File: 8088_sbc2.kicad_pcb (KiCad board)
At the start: 2 copper layers, 200 x 100 mm, 65 parts, among them P1 CONN_02X10, P2 JMP_USB_PWR, P3 USB_B, Q1 IRLML6402, SW1 SW_PUSH, U1 P8088, U11 74HC573, U12 74HC573, U13 74HC573, U14 74HC573, U15 74HC138, U16 74HC138, U17 74HC14_OWN, U18 74HC08, U19 74HC32, U2 28C64, U20 10xLEDBAR, U3 AS6C4008, U4 TL770xA, U5 16C550, U6 FT232RL, U7 OSC_SMALL

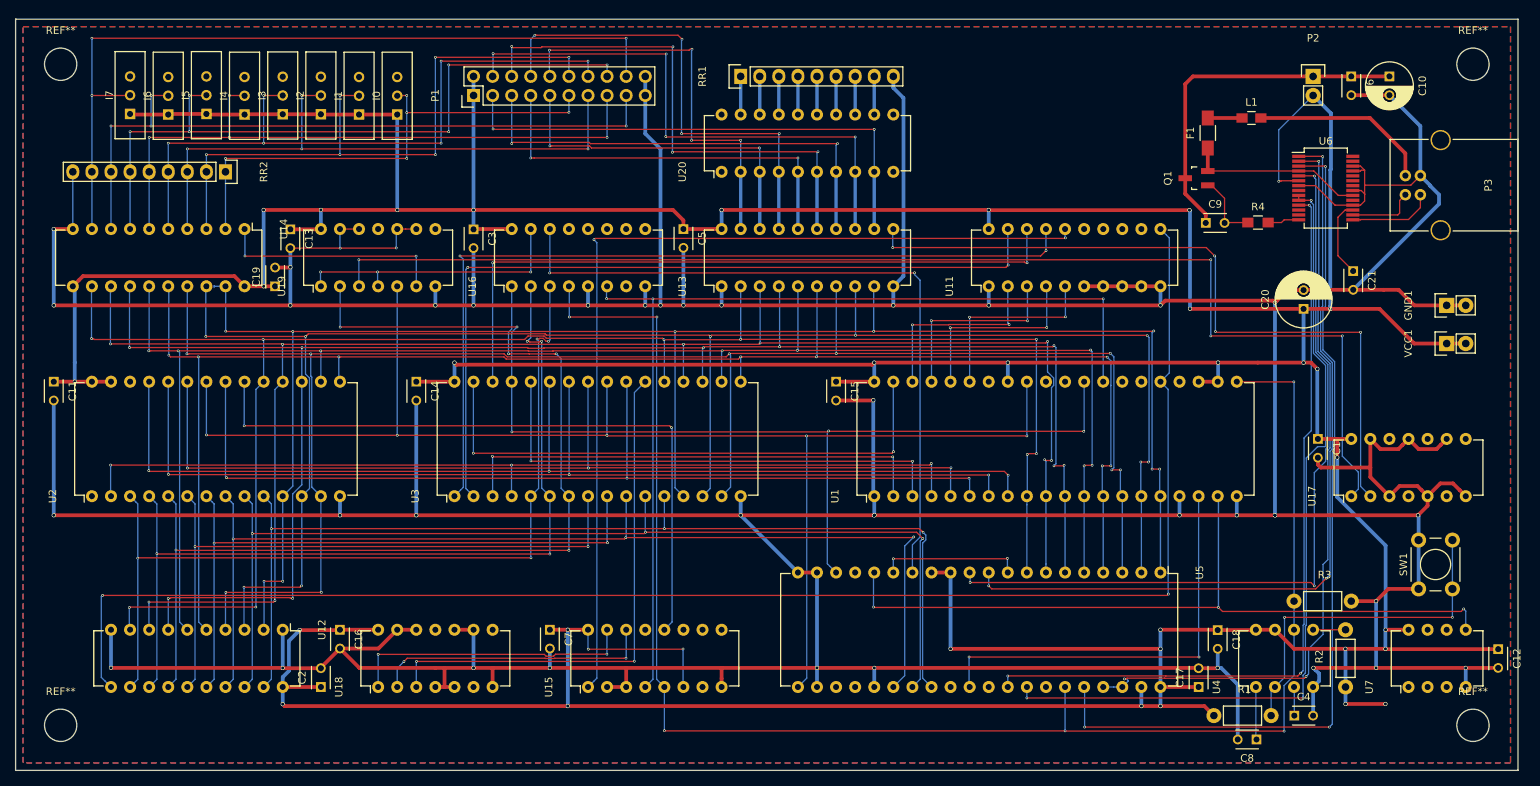
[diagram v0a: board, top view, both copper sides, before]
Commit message: version with new design rules
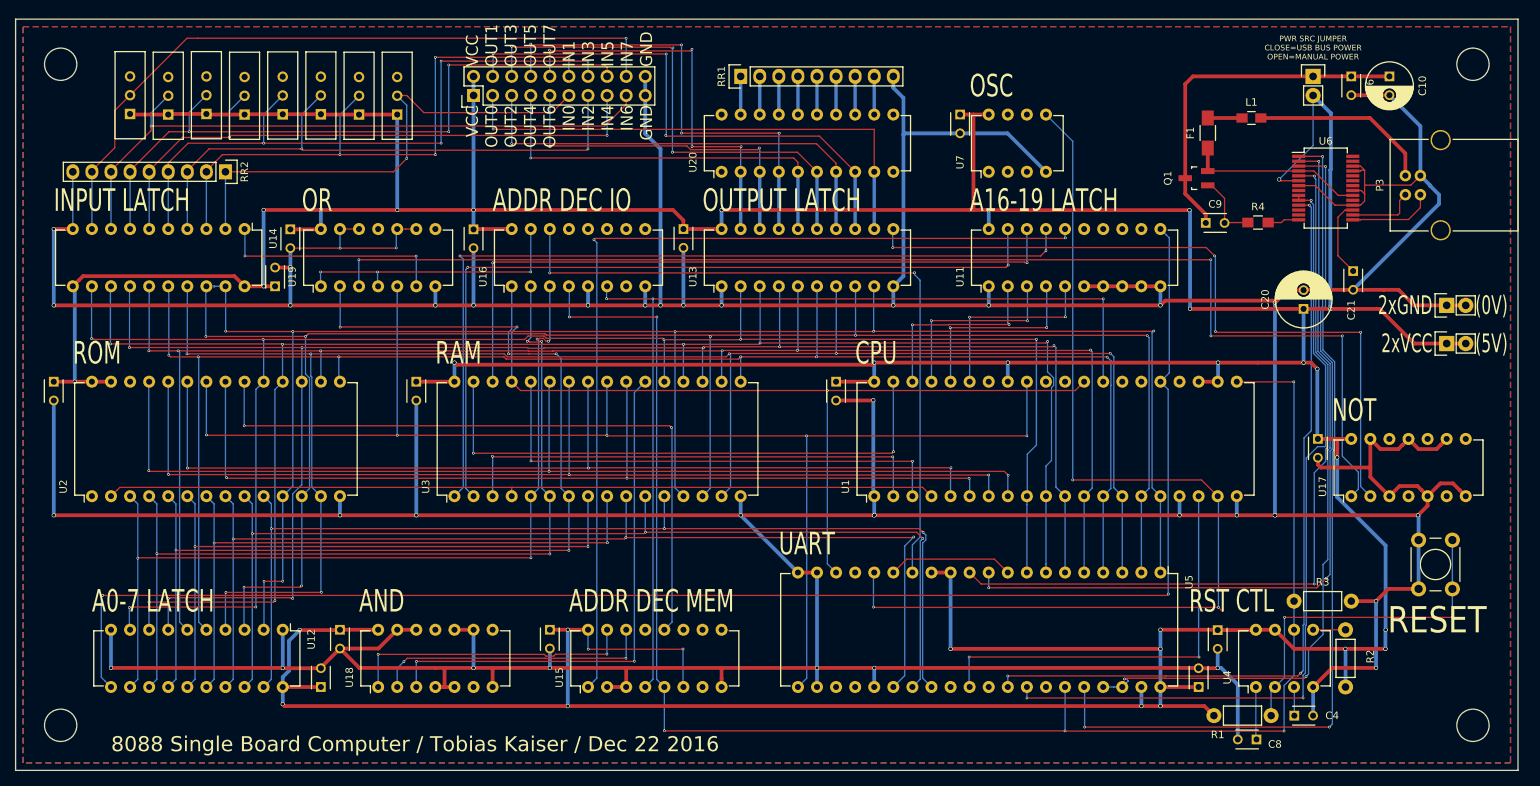
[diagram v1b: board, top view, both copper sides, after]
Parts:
- moved C12 101.0 mm to (175.7, 62.7)
- moved U7 88.5 mm to (179.5, 70.3)
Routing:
- net /CLK: track 101.3 -> 136.5 mm
- net /IN7: track 106.7 -> 94.2 mm, vias 3 -> 1
- net /A12: track 122.0 -> 111.5 mm, vias 3 -> 0
- net VCC: track 863.3 -> 853.9 mm, vias 35 -> 33
- net /nWR: track 145.5 -> 138.5 mm, vias 5 -> 3
- net /IN6: track 92.7 -> 86.6 mm, vias 4 -> 1
- net /IN5: track 94.0 -> 89.5 mm, vias 6 -> 3
- net /IN4: track 86.4 -> 82.4 mm, vias 4 -> 2
- net /IN2: track 80.8 -> 77.7 mm, vias 4 -> 2
- net /IN3: track 89.2 -> 86.1 mm, vias 6 -> 4
- net /OUT1: track 74.7 -> 71.9 mm, vias 4 -> 3
- net /IN1: track 84.1 -> 81.4 mm, vias 6 -> 4
- net Net-(U5-Pad15): track 18.9 -> 16.8 mm, vias 2 -> 0
- net /OUT2: track 61.4 -> 59.4 mm, vias 2 -> 1
- net /OUT3: track 69.4 -> 67.5 mm, vias 4 -> 3
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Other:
- net class Default: clearance 0.15 -> 0.16; trace_width 0.15 -> 0.16; via_dia 0.35 -> 0.45; via_drill 0.2 -> 0.3
- rule trace_clearance: 0.15 -> 0.16
- rule trace_min: 0.15 -> 0.16
- rule via_min_drill: 0.2 -> 0.3
- rule via_min_size: 0.35 -> 0.45
- board text added: "(0V)"
- board text added: "(5V)"
- board text added: "2xGND"
- board text added: "2xVCC"
- board text added: "8088 Single Board Computer / Tobias Kaiser / Dec 22 2016"
- board text added: "A0-7 LATCH"
- board text added: "A16-19 LATCH"
- board text added: "ADDR DEC IO"
- board text added: "ADDR DEC MEM"
- board text added: "AND"
- board text added: "CPU"
- board text added: "INPUT LATCH"
- board text added: "NOT"
- board text added: "OR"
- board text added: "OSC"
- board text added: "OUTPUT LATCH"
- board text added: "PWR SRC JUMPER CLOSE=USB BUS POWER OPEN=MANUAL POWER"
- board text added: "RAM"
- board text added: "RESET"
- board text added: "ROM"
- board text added: "RST CTL"
- board text added: "UART"
- board text added: "VCC OUT0 OUT2 OUT4 OUT6 IN0 IN2 IN4 IN6 GND"
- board text added: "VCC OUT1 OUT3 OUT5 OUT7 IN1 IN3 IN5 IN7 GND"

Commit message: test
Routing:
- net GND: track 1033.4 -> 0.00 mm, vias 38 -> 0
- net VCC: track 853.9 -> 0.00 mm, vias 33 -> 0
- net /D2: track 241.0 -> 0.00 mm, vias 7 -> 0
- net /D1: track 240.1 -> 0.00 mm, vias 7 -> 0
- net /D0: track 235.4 -> 0.00 mm, vias 7 -> 0
- net /D7: track 233.4 -> 0.00 mm, vias 7 -> 0
- net /D6: track 231.8 -> 0.00 mm, vias 7 -> 0
- net /D4: track 218.7 -> 0.00 mm, vias 6 -> 0
- net /D3: track 216.8 -> 0.00 mm, vias 6 -> 0
- net /RES: track 214.3 -> 0.00 mm, vias 6 -> 0
- net /ALE: track 204.8 -> 0.00 mm, vias 2 -> 0
- net /nRD: track 184.5 -> 0.00 mm, vias 5 -> 0
- net /nIODEV0_WREN: track 167.2 -> 0.00 mm, vias 4 -> 0
- net /A2: track 143.6 -> 0.00 mm, vias 3 -> 0
- net /A8: track 141.3 -> 0.00 mm, vias 3 -> 0
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- removed copper zone on B.Cu, net GND
- removed copper zone on F.Cu, net GND

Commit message: shitty kicad fucked it up while saving. fuck it.
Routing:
- net GND: track 0.00 -> 1033.4 mm, vias 0 -> 38
- net VCC: track 0.00 -> 853.9 mm, vias 0 -> 33
- net /D2: track 0.00 -> 241.0 mm, vias 0 -> 7
- net /D1: track 0.00 -> 240.1 mm, vias 0 -> 7
- net /D0: track 0.00 -> 235.4 mm, vias 0 -> 7
- net /D7: track 0.00 -> 233.4 mm, vias 0 -> 7
- net /D6: track 0.00 -> 231.8 mm, vias 0 -> 7
- net /D4: track 0.00 -> 218.7 mm, vias 0 -> 6
- net /D3: track 0.00 -> 216.8 mm, vias 0 -> 6
- net /RES: track 0.00 -> 214.3 mm, vias 0 -> 6
- net /ALE: track 0.00 -> 204.8 mm, vias 0 -> 2
- net /nRD: track 0.00 -> 184.5 mm, vias 0 -> 5
- net /nIODEV0_WREN: track 0.00 -> 167.2 mm, vias 0 -> 4
- net /A2: track 0.00 -> 143.6 mm, vias 0 -> 3
- net /A8: track 0.00 -> 141.3 mm, vias 0 -> 3
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- added copper zone on B.Cu, net GND
- added copper zone on F.Cu, net GND

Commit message: zwischenstand
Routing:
- net Net-(U5-Pad36): track 117.2 -> 38.5 mm, vias 3 -> 2
- net Net-(U5-Pad10): track 108.0 -> 51.5 mm
- net (no net): track 0.04 -> 5.97 mm
- net /A7: track 117.4 -> 115.9 mm, vias 4 -> 2
- net /A6: track 116.9 -> 116.2 mm
- net VCC: track 853.9 -> 854.5 mm, vias 33 -> 32
- net /A17: track 91.6 -> 92.1 mm
- removed copper zone on B.Cu, net GND
- removed copper zone on F.Cu, net GND

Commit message: zwischenstand2
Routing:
- net Net-(U5-Pad36): track 38.5 -> 115.8 mm, vias 2 -> 4
- net (no net): track 5.97 -> 0.04 mm
- net /ALE: track 204.8 -> 208.6 mm
- net Net-(U5-Pad37): track 102.1 -> 103.0 mm

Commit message: zwischenstand3
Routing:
- net VCC: track 854.5 -> 840.9 mm, vias 32 -> 26
- net GND: track 1033.6 -> 1027.5 mm, vias 38 -> 30
- net /OUT0: track 68.5 -> 64.6 mm
- net /A19: track 124.3 -> 122.3 mm, vias 2 -> 1
- net /D0: track 235.6 -> 233.8 mm
- net /nIODEV0_RDEN: track 30.4 -> 28.7 mm
- net /A12: track 111.5 -> 112.8 mm
- net /OUT7: track 53.1 -> 51.8 mm, vias 4 -> 2
- net /nIODEV0_EN: track 37.7 -> 36.7 mm, vias 3 -> 1
- net /OUT6: track 45.9 -> 44.9 mm, vias 2 -> 1
- net /A18: track 113.9 -> 113.0 mm
- net /IN6: track 86.6 -> 85.9 mm

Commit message: zwischenstand5
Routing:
- net /A2: track 143.6 -> 141.2 mm
- net /A0: track 139.1 -> 141.4 mm
- net /A1: track 141.1 -> 140.3 mm
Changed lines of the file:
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@@
   (via (at 128.7908 119.6976) (size 0.45) (drill 0.3) (layers F.Cu B.Cu) (net 84))
   (segment (start 76.199999 114.299999) (end 75.4 113.5) (width 0.16) (layer B.Cu) (net 84))
+  (segment (start 167.362298 119.1388) (end 168.354999 120.131501) (width 0.16) (layer F.Cu) (net 85))
+  (segment (start 167.2972 119.073702) (end 167.362298 119.1388) (width 0.16) (layer F.Cu) (net 85))
+  (segment (start 131.2292 119.0118) (end 166.6876 119.0118) (width 0.16) (layer F.Cu) (net 85))
+  (segment (start 167.362298 119.1388) (end 167.235298 119.0118) (width 0.16) (layer F.Cu) (net 85))
+  (segment (start 167.235298 119.0118) (end 166.6876 119.0118) (width 0.16) (layer F.Cu) (net 85))
+  (via (at 168.354999 120.131501) (size 0.45) (drill 0.3) (layers F.Cu B.Cu) (net 85))
   (segment (start 77.94 138.9) (end 78.980001 137.859999) (width 0.16) (layer B.Cu) (net 85))
   (segment (start 78.980001 137.859999) (end 78.980001 119.522798) (width 0.16) (layer B.Cu) (net 85))
   (segment (start 78.980001 119.522798) (end 78.965001 119.507798) (width 0.16) (layer B.Cu) (net 85))
   (segment (start 78.965001 119.507798) (end 78.965001 119.1896) (width 0.16) (layer B.Cu) (net 85))
-  (segment (start 131.2292 119.0118) (end 169.4747 119.0118) (width 0.16) (layer F.Cu) (net 85))
-  (segment (start 169.384929 119.101571) (end 169.559928 118.926572) (width 0.16) (layer B.Cu) (net 85))
-  (segment (start 168.354999 120.131501) (end 169.384929 119.101571) (width 0.16) (layer B.Cu) (net 85))
   (segment (start 168.354999 137.385001) (end 168.354999 120.131501) (width 0.16) (layer B.Cu) (net 85))
   (segment (start 166.84 138.9) (end 168.354999 137.385001) (width 0.16) (layer B.Cu) (net 85))
-  (segment (start 169.4747 119.0118) (end 169.559928 118.926572) (width 0.16) (layer F.Cu) (net 85))
-  (via (at 169.559928 118.926572) (size 0.45) (drill 0.3) (layers F.Cu B.Cu) (net 85))
   (segment (start 78.965001 119.1896) (end 78.965001 114.525001) (width 0.16) (layer B.Cu) (net 85))
   (segment (start 131.2292 119.0118) (end 131.0514 119.1896) (width 0.16) (layer F.Cu) (net 85))
@@
   (segment (start 78.965001 114.525001) (end 78.739999 114.299999) (width 0.16) (layer B.Cu) (net 85))
   (segment (start 78.739999 114.299999) (end 77.94 113.5) (width 0.16) (layer B.Cu) (net 85))
+  (segment (start 169.38 138.9) (end 170.423719 137.856281) (width 0.16) (layer B.Cu) (net 86))
+  (segment (start 170.423719 137.856281) (end 170.42485 137.85515) (width 0.16) (layer B.Cu) (net 86))
+  (segment (start 170.42485 119.7992) (end 170.42485 137.58025) (width 0.16) (layer B.Cu) (net 86))
+  (segment (start 170.42485 137.58025) (end 170.418822 137.586278) (width 0.16) (layer B.Cu) (net 86))
+  (segment (start 170.418822 137.586278) (end 170.418822 137.851384) (width 0.16) (layer B.Cu) (net 86))
+  (segment (start 170.418822 137.851384) (end 170.423719 137.856281) (width 0.16) (layer B.Cu) (net 86))
+  (segment (start 133.8454 118.3006) (end 169.126 118.3006) (width 0.16) (layer F.Cu) (net 86))
+  (segment (start 169.126 118.3006) (end 170.42485 119.59945) (width 0.16) (layer F.Cu) (net 86))
+  (segment (start 170.42485 119.59945) (end 170.42485 119.7992) (width 0.16) (layer F.Cu) (net 86))
+  (via (at 170.42485 119.7992) (size 0.45) (drill 0.3) (layers F.Cu B.Cu) (net 86))
   (segment (start 80.48 138.9) (end 81.520001 137.859999) (width 0.16) (layer B.Cu) (net 86))
   (segment (start 81.520001 137.859999) (end 81.520001 118.811598) (width 0.16) (layer B.Cu) (net 86))
   (segment (start 81.505001 118.796598) (end 81.505001 118.4784) (width 0.16) (layer B.Cu) (net 86))
   (segment (start 81.520001 118.811598) (end 81.505001 118.796598) (width 0.16) (layer B.Cu) (net 86))
-  (segment (start 169.9388 118.3006) (end 170.763256 119.125056) (width 0.16) (layer F.Cu) (net 86))
-  (segment (start 170.763256 119.125056) (end 170.763256 119.129937) (width 0.16) (layer F.Cu) (net 86))
-  (segment (start 169.38 138.9) (end 170.42485 137.85515) (width 0.16) (layer B.Cu) (net 86))
-  (segment (start 170.42485 137.85515) (end 170.42485 119.468343) (width 0.16) (layer B.Cu) (net 86))
-  (segment (start 170.42485 119.468343) (end 170.588257 119.304936) (width 0.16) (layer B.Cu) (net 86))
-  (via (at 170.763256 119.129937) (size 0.45) (drill 0.3) (layers F.Cu B.Cu) (net 86))
-  (segment (start 133.8454 118.3006) (end 169.9388 118.3006) (width 0.16) (layer F.Cu) (net 86))
-  (segment (start 170.588257 119.304936) (end 170.763256 119.129937) (width 0.16) (layer B.Cu) (net 86))
   (segment (start 81.505001 118.4784) (end 81.505001 114.525001) (width 0.16) (layer B.Cu) (net 86))
   (segment (start 133.8454 118.3006) (end 133.6676 118.4784) (width 0.16) (layer F.Cu) (net 86))
@@
   (segment (start 81.505001 114.525001) (end 81.279999 114.299999) (width 0.16) (layer B.Cu) (net 86))
   (segment (start 81.279999 114.299999) (end 80.48 113.5) (width 0.16) (layer B.Cu) (net 86))
+  (segment (start 136.36 117.818) (end 170.142 117.818) (width 0.16) (layer F.Cu) (net 87))
+  (segment (start 171.3612 117.818) (end 170.142 117.818) (width 0.16) (layer F.Cu) (net 87))
+  (segment (start 170.738831 137.718831) (end 173.100001 135.357661) (width 0.16) (layer B.Cu) (net 87))
+  (segment (start 173.100001 135.357661) (end 173.100001 119.556801) (width 0.16) (layer B.Cu) (net 87))
+  (segment (start 173.100001 119.556801) (end 171.3612 117.818) (width 0.16) (layer B.Cu) (net 87))
+  (via (at 171.3612 117.818) (size 0.45) (drill 0.3) (layers F.Cu B.Cu) (net 87))
   (segment (start 83.819999 138.100001) (end 83.02 138.9) (width 0.16) (layer B.Cu) (net 87))
   (segment (start 84.060001 137.859999) (end 83.819999 138.100001) (width 0.16) (layer B.Cu) (net 87))
@@
   (segment (start 83.820002 118.042999) (end 83.820002 127.586604) (width 0.16) (layer B.Cu) (net 87))
   (segment (start 84.045001 117.818) (end 83.820002 118.042999) (width 0.16) (layer B.Cu) (net 87))
-  (segment (start 170.98001 118.482273) (end 170.805011 118.307274) (width 0.16) (layer B.Cu) (net 87))
-  (segment (start 171.163258 118.665521) (end 170.98001 118.482273) (width 0.16) (layer B.Cu) (net 87))
-  (segment (start 170.630012 118.132275) (end 170.805011 118.307274) (width 0.16) (layer F.Cu) (net 87))
-  (segment (start 136.36 117.818) (end 170.315737 117.818) (width 0.16) (layer F.Cu) (net 87))
-  (segment (start 170.315737 117.818) (end 170.630012 118.132275) (width 0.16) (layer F.Cu) (net 87))
-  (via (at 170.805011 118.307274) (size 0.45) (drill 0.3) (layers F.Cu B.Cu) (net 87))
-  (segment (start 171.163258 119.321939) (end 171.163258 118.665521) (width 0.16) (layer B.Cu) (net 87))
-  (segment (start 170.738831 119.746366) (end 171.163258 119.321939) (width 0.16) (layer B.Cu) (net 87))
-  (segment (start 170.738831 137.718831) (end 170.738831 119.746366) (width 0.16) (layer B.Cu) (net 87))
   (segment (start 171.92 138.9) (end 170.738831 137.718831) (width 0.16) (layer B.Cu) (net 87))
   (segment (start 84.045001 117.818) (end 84.045001 114.525001) (width 0.16) (layer B.Cu) (net 87))

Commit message: zwischenstand
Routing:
- net GND: track 1027.5 -> 1059.6 mm, vias 30 -> 19
- net /nROMEN: track 90.2 -> 64.4 mm
- net /D1: track 240.2 -> 220.4 mm
- net VCC: track 840.9 -> 833.5 mm, vias 26 -> 21
- net Net-(R1-Pad2): track 46.5 -> 44.2 mm, vias 2 -> 1
- net /nIODEV0_RDEN: track 28.7 -> 30.8 mm, vias 2 -> 1
- net /D6: track 232.1 -> 230.8 mm, vias 7 -> 6
- net /D0: track 233.8 -> 232.6 mm, vias 7 -> 6
- net /D7: track 233.3 -> 232.2 mm, vias 7 -> 6
- net /nIODEV0_WREN: track 167.3 -> 166.4 mm
- net /IO/nM: track 130.9 -> 130.0 mm, vias 3 -> 2
- net Net-(U5-Pad33): track 109.4 -> 108.6 mm, vias 3 -> 2
- net Net-(U5-Pad32): track 105.1 -> 104.3 mm, vias 3 -> 2
- net /D2: track 241.2 -> 242.0 mm
- net /D3: track 217.2 -> 217.8 mm, vias 6 -> 5
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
